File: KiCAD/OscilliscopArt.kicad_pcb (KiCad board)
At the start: 2 copper layers, 37 x 42 mm, 6 parts, among them J1 Conn_01x09, J2 Conn_01x09, U1 MCP4902

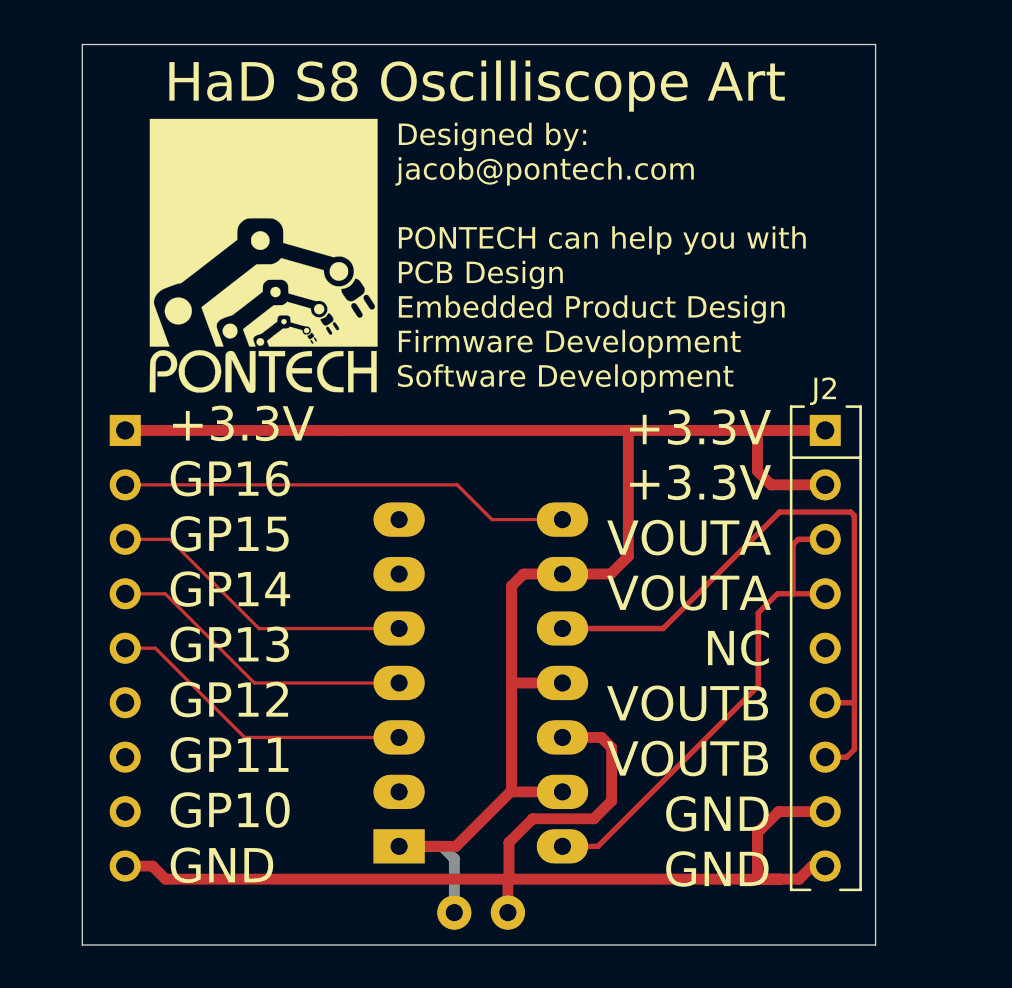
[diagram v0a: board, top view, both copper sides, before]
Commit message: Added SAO header
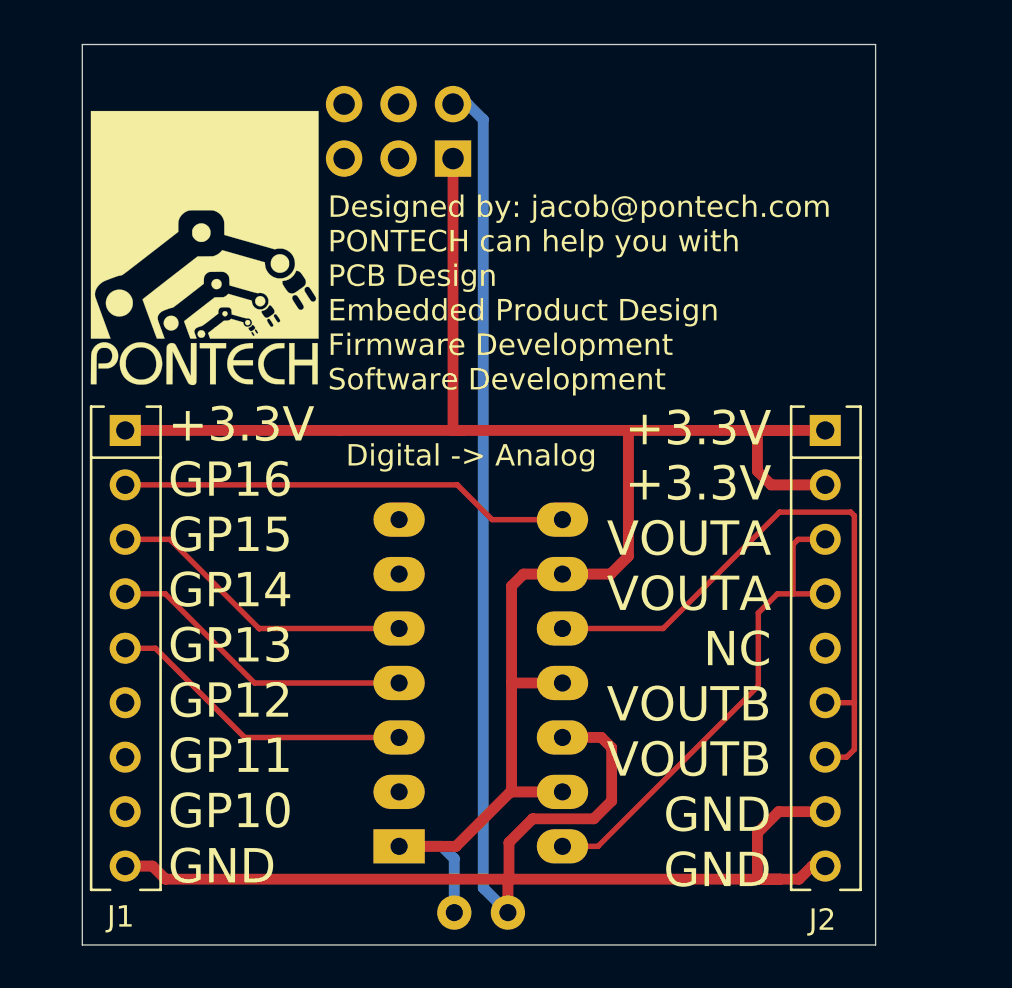
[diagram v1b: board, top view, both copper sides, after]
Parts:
- added J3: Conn_02x03_Odd_Even, Connector_PinHeader_2.54mm:PinHeader_2x03_P2.54mm_Vertical, B.Cu at (172.3, 67.3)
- J1: moved to F.Cu
- moved G*** 3.70 mm to (182.9, 70.6)
- moved ART1 2.77 mm to (160.7, 71.5)
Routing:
- net GND: track 53.8 -> 93.0 mm
- net +3V3: track 77.2 -> 90.3 mm
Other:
- board text added: "Digital -> Analog"
- board text added: "SAO"

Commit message: REV-A Gerbers + Added WEE and Open Hardware Logos
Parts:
- added REF**: OSHW-Logo2_7.3x6mm_SilkScreen, Symbol:OSHW-Logo2_7.3x6mm_SilkScreen, F.Cu at (187.0, 66.0)
- added REF**: WEEE-Logo_4.2x6mm_SilkScreen, Symbol:WEEE-Logo_4.2x6mm_SilkScreen, B.Cu at (159.3, 65.1)
- added REF**: OSHW-Logo2_7.3x6mm_SilkScreen, Symbol:OSHW-Logo2_7.3x6mm_SilkScreen, B.Cu at (169.8, 75.3)
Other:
- board text added: "Oscilliscope Art REV A"
- board text removed: "HaD S8 Oscilliscope Art"
